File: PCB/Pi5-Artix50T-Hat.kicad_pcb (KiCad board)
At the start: 4 copper layers, 65 x 56 mm, 160 parts, among them J1 GPIO, J2 Molex 0878321420, J3 68711614522, J4 Molex 0878321420, U1 BL24C256A, U10 AP62200TWU-7, U11 AP62200TWU-7, U12 AP62200TWU-7, U2 XC7A50T-FGG484, U9 AP62200TWU-7, X1 50MHz

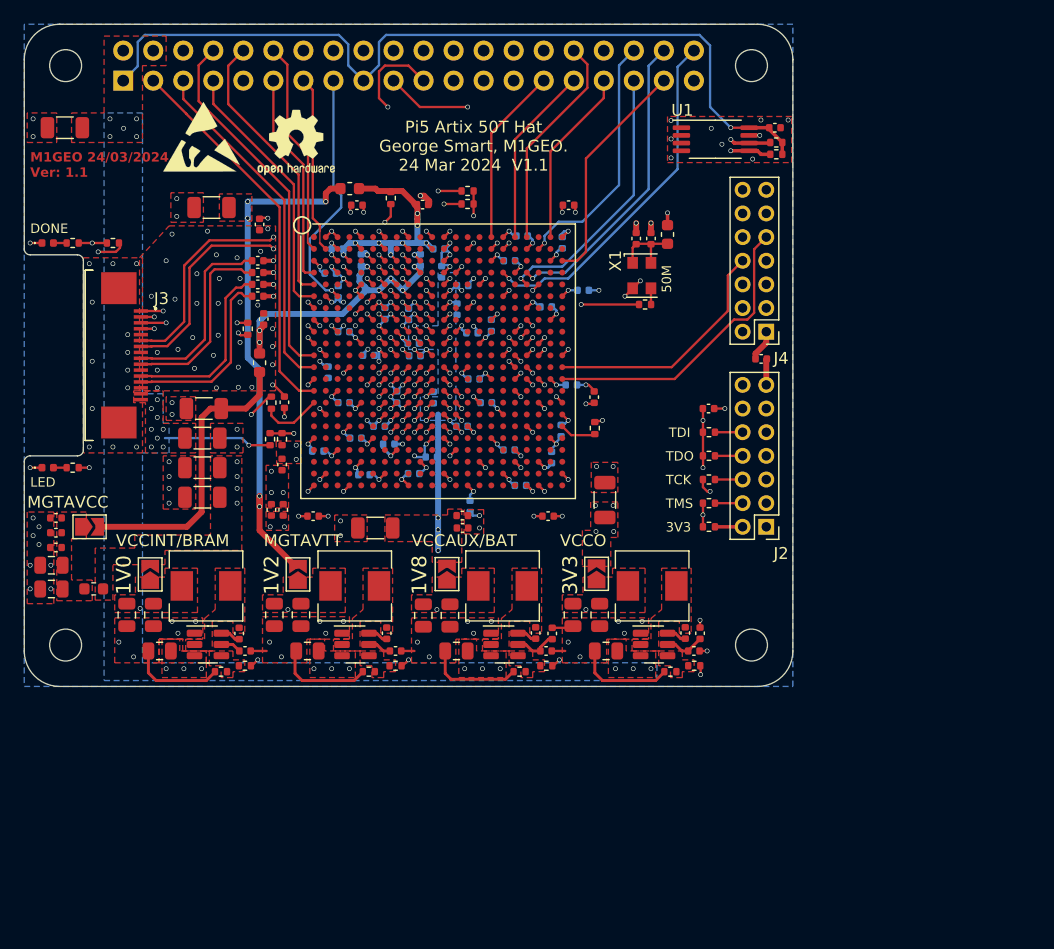
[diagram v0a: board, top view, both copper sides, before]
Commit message: Connecting and routing diff pairs
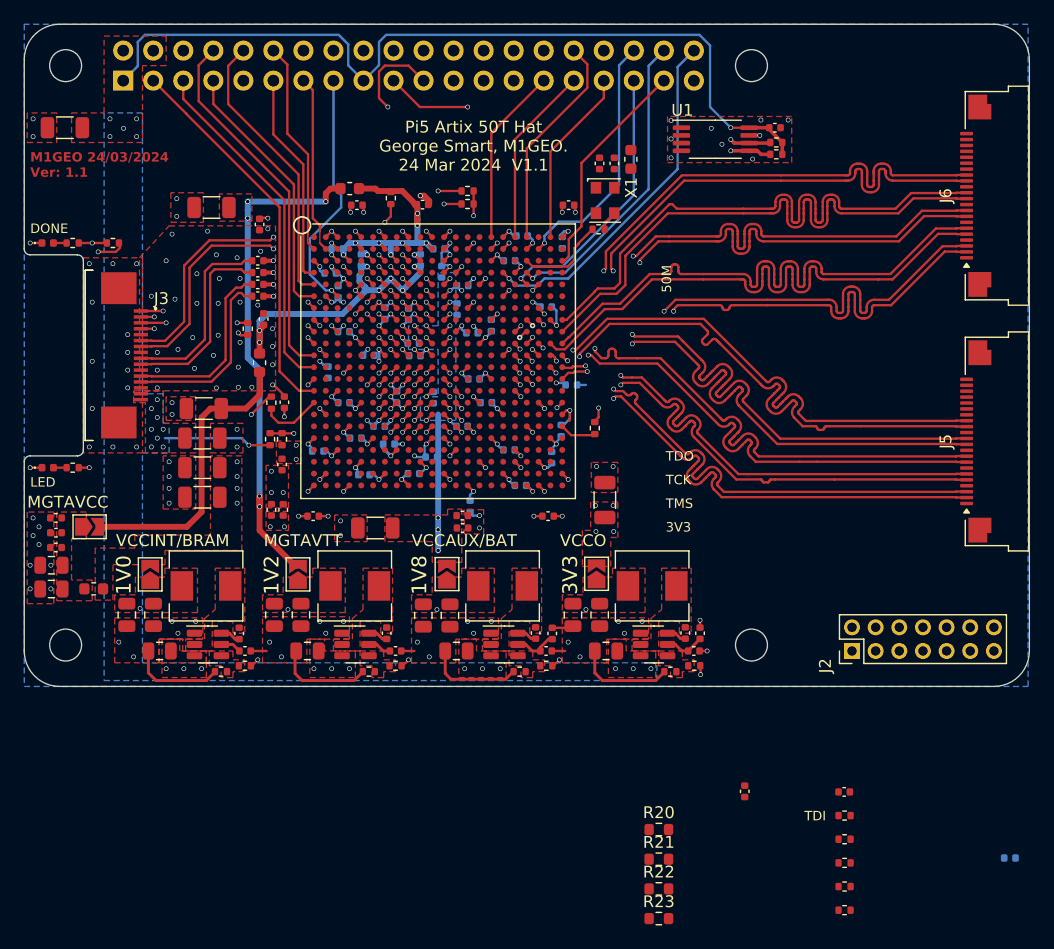
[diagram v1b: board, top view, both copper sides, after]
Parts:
- removed C22: 100n, Capacitor_SMD:C_0402_1005Metric
- removed J4: Molex 0878321420, Connector_PinHeader_2.00mm:PinHeader_2x07_P2.00mm_Vertical
- removed REF**: ESD-Logo_6.6x6mm_SilkScreen, Symbol:ESD-Logo_6.6x6mm_SilkScreen
- removed REF**: OSHW-Logo2_7.3x6mm_SilkScreen, Symbol:OSHW-Logo2_7.3x6mm_SilkScreen
- added J5: MIPI0, Connector_FFC-FPC:Amphenol_F32Q-1A7x1-11022_1x22-1MP_P0.5mm_Horizontal, F.Cu at (182.6, 79.3)
- added J6: MIPI1, Connector_FFC-FPC:Amphenol_F32Q-1A7x1-11022_1x22-1MP_P0.5mm_Horizontal, F.Cu at (182.6, 58.5)
- added R20: 0R, Resistor_SMD:R_0603_1608Metric, F.Cu at (153.7, 112.1)
- added R21: 0R, Resistor_SMD:R_0603_1608Metric, F.Cu at (153.7, 114.6)
- added R22: 0R, Resistor_SMD:R_0603_1608Metric, F.Cu at (153.7, 117.1)
- added R23: 0R, Resistor_SMD:R_0603_1608Metric, F.Cu at (153.7, 119.6)
- moved C59 60.1 mm to (183.3, 114.5)
- moved C65 35.7 mm to (160.9, 108.9)
- moved C21 34.4 mm to (169.3, 108.9)
- moved R3 34.4 mm to (169.4, 116.9)
- moved R4 34.4 mm to (169.4, 118.9)
- moved R5 34.4 mm to (169.4, 112.9)
- moved R6 34.4 mm to (169.4, 110.9)
- moved R7 34.4 mm to (169.4, 114.9)
- moved J2 12.8 mm to (170.0, 97.0), turned to 90 degrees
- moved R16 7.48 mm to (148.6, 61.3)
- moved C93 7.07 mm to (148.7, 55.8)
- moved C94 7.07 mm to (149.9, 55.8)
- moved FB3 7.07 mm to (151.3, 55.4)
- moved X1 7.07 mm to (149.1, 58.9)
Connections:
- U2 pad A17: +3V3 -> BANK_16_VCC
- U2 pad B14: +3V3 -> BANK_16_VCC
- U2 pad C19: unconnected-(U2B-IO_L13N_T2_MRCC_16-PadC19) -> /FPGA Top/CLK50MHZ
- U2 pad C21: +3V3 -> BANK_16_VCC
- U2 pad D18: +3V3 -> BANK_16_VCC
- U2 pad E15: +3V3 -> BANK_16_VCC
- U2 pad F22: +3V3 -> BANK_16_VCC
- U2 pad G19: +3V3 -> BANK_15_VCC
- U2 pad G20: unconnected-(U2B-IO_L8N_T1_AD10N_15-PadG20) -> /FPGA Top/FPGA Bank 15 & 16/MIPI1_D1-
- U2 pad H16: +3V3 -> BANK_15_VCC
- U2 pad H19: /FPGA Top/FPGA Bank 15 & 16/IOHEADER0 -> /FPGA Top/FPGA Bank 15 & 16/MIPI1_CK-
- U2 pad H20: unconnected-(U2B-IO_L8P_T1_AD10P_15-PadH20) -> /FPGA Top/FPGA Bank 15 & 16/MIPI1_D1+
- U2 pad H22: unconnected-(U2B-IO_L7N_T1_AD2N_15-PadH22) -> /FPGA Top/FPGA Bank 15 & 16/MIPI1_D2-
- U2 pad J13: +3V3 -> BANK_15_VCC
- U2 pad J19: /FPGA Top/CLK50MHZ -> /FPGA Top/FPGA Bank 15 & 16/MIPI1_CK+
- U2 pad J22: unconnected-(U2B-IO_L7P_T1_AD2P_15-PadJ22) -> /FPGA Top/FPGA Bank 15 & 16/MIPI1_D2+
- U2 pad K18: /FPGA Top/FPGA Bank 15 & 16/IOHEADER1 -> /FPGA Top/FPGA Bank 15 & 16/MIPI0_CK+
- U2 pad K19: /FPGA Top/FPGA Bank 15 & 16/IOHEADER2 -> /FPGA Top/FPGA Bank 15 & 16/MIPI0_CK-
- U2 pad K20: +3V3 -> BANK_15_VCC
- U2 pad K21: unconnected-(U2B-IO_L9P_T1_DQS_AD3P_15-PadK21) -> /FPGA Top/FPGA Bank 15 & 16/MIPI1_D3+
- U2 pad K22: unconnected-(U2B-IO_L9N_T1_DQS_AD3N_15-PadK22) -> /FPGA Top/FPGA Bank 15 & 16/MIPI1_D3-
- U2 pad L17: +3V3 -> BANK_15_VCC
- U2 pad L18: /FPGA Top/FPGA Bank 15 & 16/IOHEADER8 -> /FPGA Top/FPGA Bank 15 & 16/MIPI0_D3-
- U2 pad L19: /FPGA Top/FPGA Bank 15 & 16/IOHEADER3 -> /FPGA Top/FPGA Bank 15 & 16/MIPI0_D1+
- U2 pad L20: /FPGA Top/FPGA Bank 15 & 16/IOHEADER4 -> /FPGA Top/FPGA Bank 15 & 16/MIPI0_D1-
- U2 pad L21: unconnected-(U2B-IO_L10N_T1_AD11N_15-PadL21) -> /FPGA Top/FPGA Bank 15 & 16/MIPI1_D0-
- U2 pad M18: /FPGA Top/FPGA Bank 15 & 16/IOHEADER7 -> /FPGA Top/FPGA Bank 15 & 16/MIPI0_D3+
- U2 pad M21: unconnected-(U2B-IO_L10P_T1_AD11P_15-PadM21) -> /FPGA Top/FPGA Bank 15 & 16/MIPI1_D0+
- U2 pad M22: /FPGA Top/FPGA Bank 15 & 16/IOHEADER6 -> /FPGA Top/FPGA Bank 15 & 16/MIPI0_D2-
- U2 pad N18: /FPGA Top/FPGA Bank 15 & 16/IOHEADER9 -> /FPGA Top/FPGA Bank 15 & 16/MIPI0_D0+
- U2 pad N19: /FPGA Top/FPGA Bank 15 & 16/IOHEADER10 -> /FPGA Top/FPGA Bank 15 & 16/MIPI0_D0-
- U2 pad N20: /FPGA Top/FPGA Bank 15 & 16/IOHEADER11 -> unconnected-(U2B-IO_L18P_T2_A24_15-PadN20)
- U2 pad N21: +3V3 -> BANK_15_VCC
- U2 pad N22: /FPGA Top/FPGA Bank 15 & 16/IOHEADER5 -> /FPGA Top/FPGA Bank 15 & 16/MIPI0_D2+
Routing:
- net /FPGA Top/FPGA Bank 15 & 16/MIPI1_D2-: track 0.00 -> 49.9 mm
- net /FPGA Top/FPGA Bank 15 & 16/MIPI1_D2+: track 0.00 -> 49.8 mm
- net /FPGA Top/FPGA Bank 15 & 16/MIPI1_D3+: track 0.00 -> 49.8 mm
- net /FPGA Top/FPGA Bank 15 & 16/MIPI1_D3-: track 0.00 -> 49.7 mm
- net /FPGA Top/FPGA Bank 15 & 16/MIPI1_CK+: track 0.00 -> 49.3 mm, vias 0 -> 2
- net /FPGA Top/FPGA Bank 15 & 16/MIPI0_D1+: track 0.00 -> 49.2 mm, vias 0 -> 2
- net /FPGA Top/FPGA Bank 15 & 16/MIPI0_D2+: track 0.00 -> 47.1 mm, vias 0 -> 2
- net /FPGA Top/FPGA Bank 15 & 16/MIPI1_D0-: track 0.00 -> 47.1 mm, vias 0 -> 2
- net /FPGA Top/FPGA Bank 15 & 16/MIPI0_D3-: track 0.00 -> 47.1 mm, vias 0 -> 2
- net /FPGA Top/FPGA Bank 15 & 16/MIPI0_CK+: track 0.00 -> 47.1 mm, vias 0 -> 2
- net /FPGA Top/FPGA Bank 15 & 16/MIPI0_D0+: track 0.00 -> 47.1 mm, vias 0 -> 2
- net /FPGA Top/FPGA Bank 15 & 16/MIPI1_D1-: track 0.00 -> 47.1 mm, vias 0 -> 2
- net /FPGA Top/FPGA Bank 15 & 16/MIPI0_D1-: track 0.00 -> 47.1 mm, vias 0 -> 2
- net /FPGA Top/FPGA Bank 15 & 16/MIPI1_CK-: track 0.00 -> 47.1 mm, vias 0 -> 2
- net /FPGA Top/FPGA Bank 15 & 16/MIPI0_D3+: track 0.00 -> 47.1 mm, vias 0 -> 2
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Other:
- board size 65 x 56 mm -> 85 x 56 mm

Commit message: connecting JTAG and other non diff pins, routing
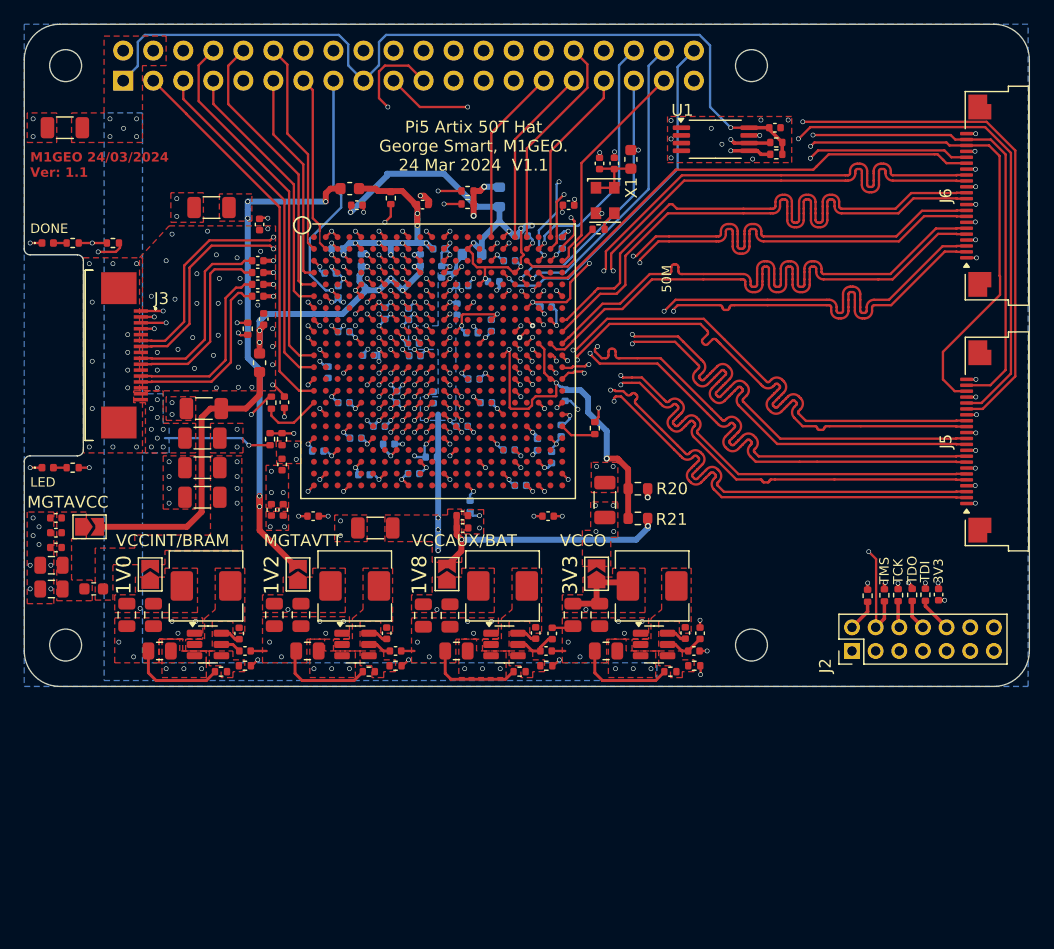
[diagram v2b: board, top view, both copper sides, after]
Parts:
- C65, R22, R23: moved to B.Cu
- moved C59 65.4 mm to (139.7, 65.8)
- moved R22 60.0 mm to (140.2, 58.6), turned to 90 degrees
- moved R23 58.3 mm to (137.9, 63.5), turned to 180 degrees
- moved C65 34.2 mm to (143.4, 79.5), turned to 90 degrees
- moved R20 28.9 mm to (151.9, 83.3)
- moved R21 28.9 mm to (151.9, 85.8)
- moved R4 26.7 mm to (171.3, 92.3), turned to 90 degrees
- moved R3 24.9 mm to (172.7, 92.3), turned to 90 degrees
- moved R7 23.1 mm to (173.9, 92.3), turned to -90 degrees
- moved R5 21.4 mm to (175.1, 92.3), turned to 90 degrees
- moved R6 19.9 mm to (176.2, 92.2), turned to 90 degrees
- moved C21 18.5 mm to (177.3, 92.2), turned to 90 degrees
- moved C49 1.02 mm to (145.7, 75.4), turned to 90 degrees
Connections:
- C38 pad 2: +3V3 -> BANK_15_VCC
- C47 pad 2: +3V3 -> BANK_15_VCC
- C48 pad 2: +3V3 -> BANK_15_VCC
- C49 pad 2: +3V3 -> BANK_15_VCC
- C50 pad 2: +3V3 -> BANK_15_VCC
- C53 pad 2: +3V3 -> BANK_16_VCC
- C58 pad 2: +3V3 -> BANK_16_VCC
- C59 pad 2: +3V3 -> BANK_16_VCC
- C66 pad 2: +3V3 -> BANK_16_VCC
- C67 pad 2: +3V3 -> BANK_16_VCC
- J5 pad 1: unconnected-(J5-Pin_1-Pad1) -> GND
- J5 pad 10: unconnected-(J5-Pin_10-Pad10) -> GND
- J5 pad 13: unconnected-(J5-Pin_13-Pad13) -> GND
- J5 pad 16: unconnected-(J5-Pin_16-Pad16) -> GND
- J5 pad 17: unconnected-(J5-Pin_17-Pad17) -> /FPGA Top/FPGA Bank 15 & 16/MIPI0_CAM_GPIO0
- J5 pad 18: unconnected-(J5-Pin_18-Pad18) -> /FPGA Top/FPGA Bank 15 & 16/MIPI0_CAM_GPIO1
- J5 pad 19: unconnected-(J5-Pin_19-Pad19) -> GND
- J5 pad 20: unconnected-(J5-Pin_20-Pad20) -> /FPGA Top/FPGA Bank 15 & 16/SCL0
- J5 pad 21: unconnected-(J5-Pin_21-Pad21) -> /FPGA Top/FPGA Bank 15 & 16/SDA0
- J5 pad 22: unconnected-(J5-Pin_22-Pad22) -> BANK_15_VCC
- J5 pad 4: unconnected-(J5-Pin_4-Pad4) -> GND
- J5 pad 7: unconnected-(J5-Pin_7-Pad7) -> GND
- J6 pad 1: unconnected-(J6-Pin_1-Pad1) -> GND
- J6 pad 10: unconnected-(J6-Pin_10-Pad10) -> GND
- J6 pad 13: unconnected-(J6-Pin_13-Pad13) -> GND
- J6 pad 16: unconnected-(J6-Pin_16-Pad16) -> GND
- J6 pad 17: unconnected-(J6-Pin_17-Pad17) -> /FPGA Top/FPGA Bank 15 & 16/MIPI1_CAM_GPIO0
- J6 pad 18: unconnected-(J6-Pin_18-Pad18) -> /FPGA Top/FPGA Bank 15 & 16/MIPI1_CAM_GPIO1
- J6 pad 19: unconnected-(J6-Pin_19-Pad19) -> GND
- J6 pad 20: unconnected-(J6-Pin_20-Pad20) -> /FPGA Top/FPGA Bank 15 & 16/SCL0
- J6 pad 21: unconnected-(J6-Pin_21-Pad21) -> /FPGA Top/FPGA Bank 15 & 16/SDA0
- J6 pad 22: unconnected-(J6-Pin_22-Pad22) -> BANK_15_VCC
- J6 pad 4: unconnected-(J6-Pin_4-Pad4) -> GND
- J6 pad 7: unconnected-(J6-Pin_7-Pad7) -> GND
- U2 pad B21: unconnected-(U2B-IO_L21P_T3_DQS_16-PadB21) -> /FPGA Top/FPGA Bank 15 & 16/SCL0
- U2 pad B22: unconnected-(U2B-IO_L20N_T3_16-PadB22) -> /FPGA Top/FPGA Bank 15 & 16/MIPI1_CAM_GPIO1
- U2 pad C20: unconnected-(U2B-IO_L19N_T3_VREF_16-PadC20) -> /FPGA Top/FPGA Bank 15 & 16/SDA0
- U2 pad D20: unconnected-(U2B-IO_L19P_T3_16-PadD20) -> /FPGA Top/FPGA Bank 15 & 16/MIPI1_CAM_GPIO0
- U2 pad F19: unconnected-(U2B-IO_L18P_T2_16-PadF19) -> /FPGA Top/FPGA Bank 15 & 16/MIPI0_CAM_GPIO0
- U2 pad F20: unconnected-(U2B-IO_L18N_T2_16-PadF20) -> /FPGA Top/FPGA Bank 15 & 16/MIPI0_CAM_GPIO1
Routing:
- net BANK_15_VCC: track 1.24 -> 118.8 mm, vias 2 -> 10
- net /FPGA Top/FPGA Bank 15 & 16/MIPI0_CAM_GPIO0: track 0.00 -> 79.1 mm, vias 0 -> 2
- net /FPGA Top/FPGA Bank 15 & 16/MIPI0_CAM_GPIO1: track 0.00 -> 76.7 mm, vias 0 -> 2
- net /FPGA Top/FPGA Bank 15 & 16/SDA0: track 0.00 -> 69.9 mm, vias 0 -> 3
- net /FPGA Top/FPGA Bank 15 & 16/SCL0: track 0.00 -> 67.5 mm, vias 0 -> 2
- net BANK_16_VCC: track 1.41 -> 51.1 mm, vias 2 -> 9
- net /FPGA Top/FPGA Bank 15 & 16/MIPI1_CAM_GPIO0: track 0.00 -> 41.0 mm
- net /FPGA Top/FPGA Bank 15 & 16/MIPI1_CAM_GPIO1: track 0.00 -> 39.2 mm, vias 0 -> 2
- net TDI: track 25.3 -> 53.0 mm
- net +1V8: track 17.1 -> 43.2 mm, vias 10 -> 12
- net TDO: track 25.3 -> 49.1 mm
- net TMS: track 25.7 -> 48.9 mm, vias 1 -> 2
- net TCK: track 26.7 -> 47.4 mm
- net GND: track 150.2 -> 165.6 mm, vias 209 -> 231
- net Net-(JP12-A): track 16.0 -> 23.0 mm
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
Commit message: Version 1.2 routed
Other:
- board text added: "17 Jul 2024 - V1.2 - Pi5 Artix 50T Hat"
- board text added: "Pi5 Artix 50T Hat Intergalaktik d.o.o. 17 Jul 2025 V1.2"
- board text removed: "24 Mar 2024 - V1.1 - Pi5 Artix 50T Hat"
- board text removed: "Pi5 Artix 50T Hat George Smart, M1GEO. 24 Mar 2024 V1.1"
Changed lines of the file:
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@@
 		(tags "capacitor")
 		(property "Reference" "C65"
-			(at 0 1.16 -90)
+			(at 0 1.16 270)
 			(layer "B.SilkS")
 			(hide yes)
@@
 		)
 		(property "Value" "4.7u"
-			(at 0 -1.16 -90)
+			(at 0 -1.16 270)
 			(layer "B.Fab")
 			(effects
@@
 		)
 		(property "Datasheet" "https://datasheet.lcsc.com/lcsc/2304140030_Samsung-Electro-Mechanics-CL05A475MP5NRNC_C23733.pdf"
-			(at 0 0 -90)
+			(at 0 0 270)
 			(unlocked yes)
 			(layer "B.Fab")
@@
 		)
 		(property "Description" ""
-			(at 0 0 -90)
+			(at 0 0 270)
 			(unlocked yes)
 			(layer "B.Fab")
@@
 		)
 		(fp_text user "${REFERENCE}"
-			(at 0 0 -90)
+			(at 0 0 270)
 			(layer "B.Fab")
 			(effects
@@
 		)
 	)
-	(gr_text "Pi5 Artix 50T Hat\nGeorge Smart, M1GEO.\n24 Mar 2024  V1.1"
+	(gr_text "Pi5 Artix 50T Hat\nIntergalaktik d.o.o.\n17 Jul 2025  V1.2"
 		(at 138 56.5 0)
 		(layer "F.SilkS")
@@
 		)
 	)
-	(gr_text "24 Mar 2024 - V1.1 - Pi5 Artix 50T Hat"
+	(gr_text "17 Jul 2024 - V1.2 - Pi5 Artix 50T Hat"
 		(at 150 99.25 0)
 		(layer "B.SilkS")
